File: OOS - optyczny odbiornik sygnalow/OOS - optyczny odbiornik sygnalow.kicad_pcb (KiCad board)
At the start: 2 copper layers, 72 x 78.6 mm, 126 parts, among them J1 Conn_01x02_Pin, J4 Conn_01x02_Socket, J5 Conn_Coaxial, J6 USB_C_Receptacle, Q1 SI2301CDS-T1-GE3, Q2 AOSS32334C, Q3 AOSS32334C, U1 OPA300AIDBVR, U2 OPA300AIDBVR, U3 AP3015KTR-G1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

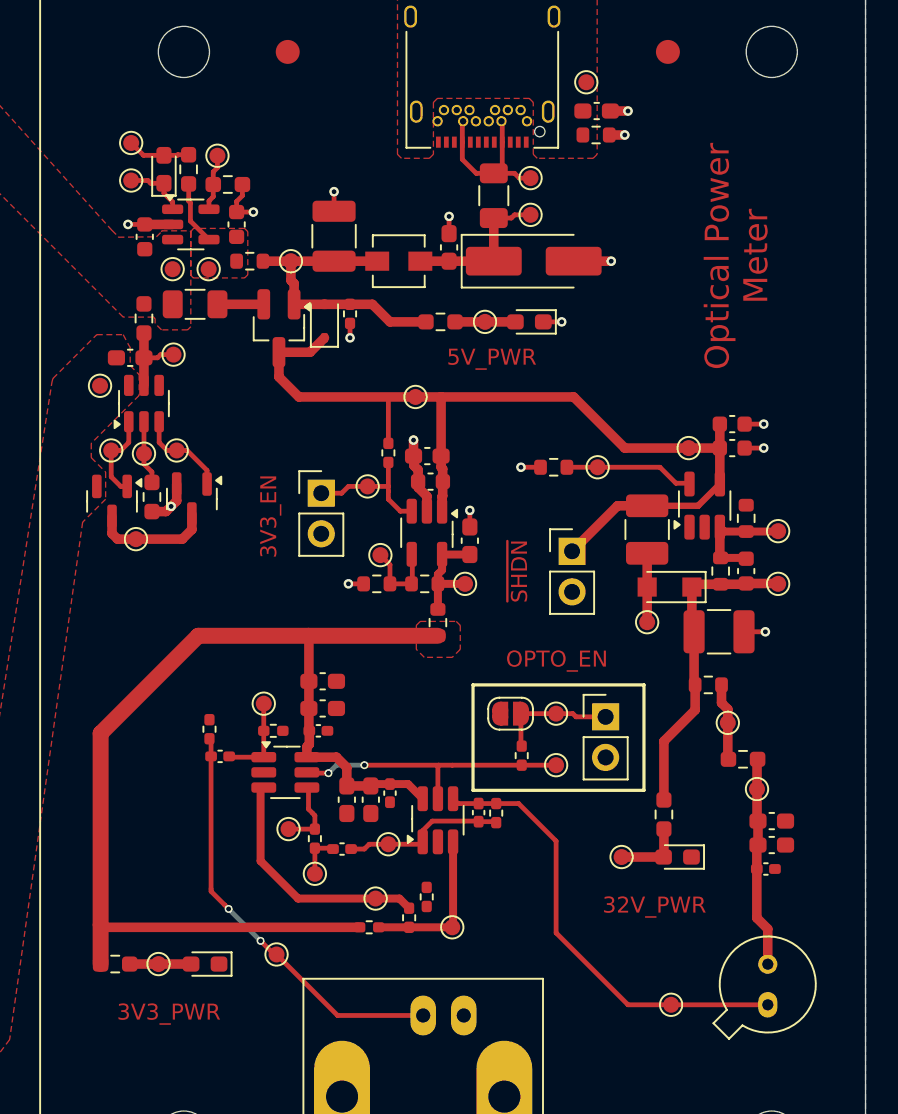
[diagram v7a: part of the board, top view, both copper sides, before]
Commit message: Layout finished, need to turn off constraints for USB (J6)
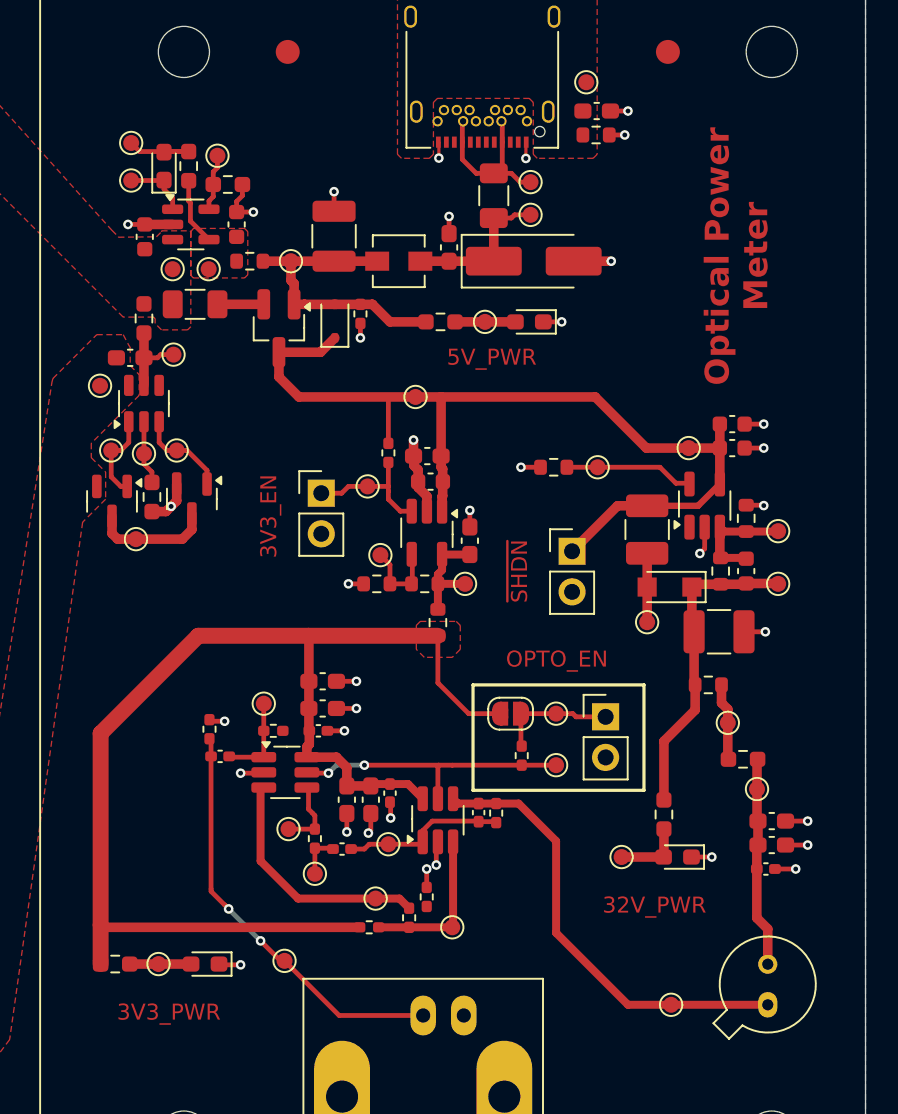
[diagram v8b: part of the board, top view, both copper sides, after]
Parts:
- moved D5 0.65 mm to (234.1, 51.8)
- moved R21 0.65 mm to (235.7, 51.4)
- moved TP11 0.64 mm to (230.9, 91.9)
- moved TP37 0.25 mm to (246.3, 43.1)
- moved D6 0.20 mm to (223.4, 42.1)
- moved R19 0.20 mm to (224.9, 42.1)
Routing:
- net 0V: track 29.1 -> 52.9 mm, vias 17 -> 36
- net +3V3: track 71.4 -> 78.8 mm
- net /Sekcja_Li-ion_Ladowanie/D5_A: track 3.93 -> 5.38 mm
- net +V_DCDC_BOOST: track 58.9 -> 59.5 mm
